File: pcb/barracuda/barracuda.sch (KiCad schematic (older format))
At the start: 79 parts, among them SW1 SW_PUSH, SW10 SW_PUSH, SW11 SW_PUSH, SW12 SW_PUSH, SW13 SW_PUSH, SW14 SW_PUSH, SW15 SW_PUSH, SW16 SW_PUSH, SW17 SW_PUSH, SW18 SW_PUSH, SW19 SW_PUSH, SW2 SW_PUSH, SW20 SW_PUSH, SW21 SW_PUSH, SW22 SW_PUSH, SW23 SW_PUSH, SW24 SW_PUSH, SW25 SW_PUSH, SW26 SW_PUSH, SW27 SW_PUSH, SW28 SW_PUSH, SW29 SW_PUSH, SW3 SW_PUSH, SW30 SW_PUSH, SW31 SW_PUSH, SW32 SW_PUSH, SW33 SW_PUSH, SW34 SW_PUSH, SW35 SW_PUSH, SW36 SW_PUSH, SW37 SW_PUSH, SW38 SW_PUSH, SW4 SW_PUSH, SW5 SW_PUSH, SW6 SW_PUSH, SW7 SW_PUSH, SW8 SW_PUSH, SW9 SW_PUSH, U1 ProMicro

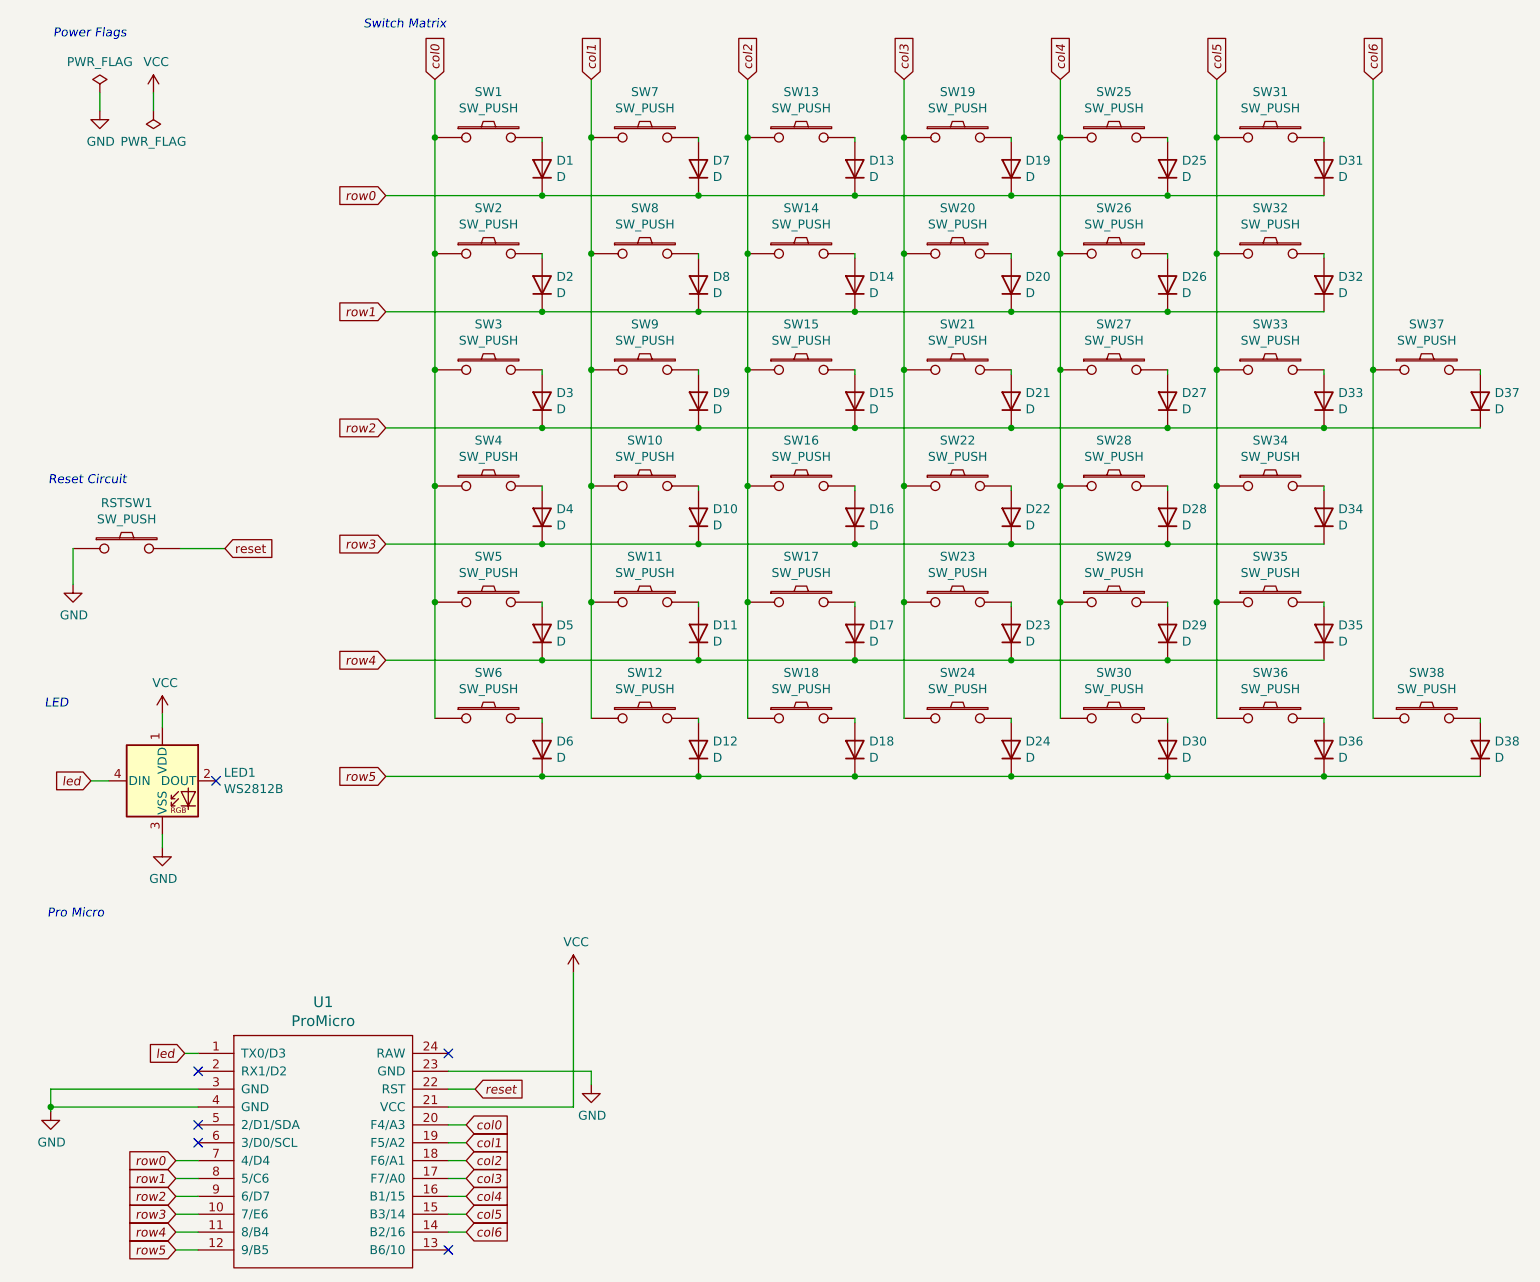
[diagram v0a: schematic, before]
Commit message: Reduced to 33 keys
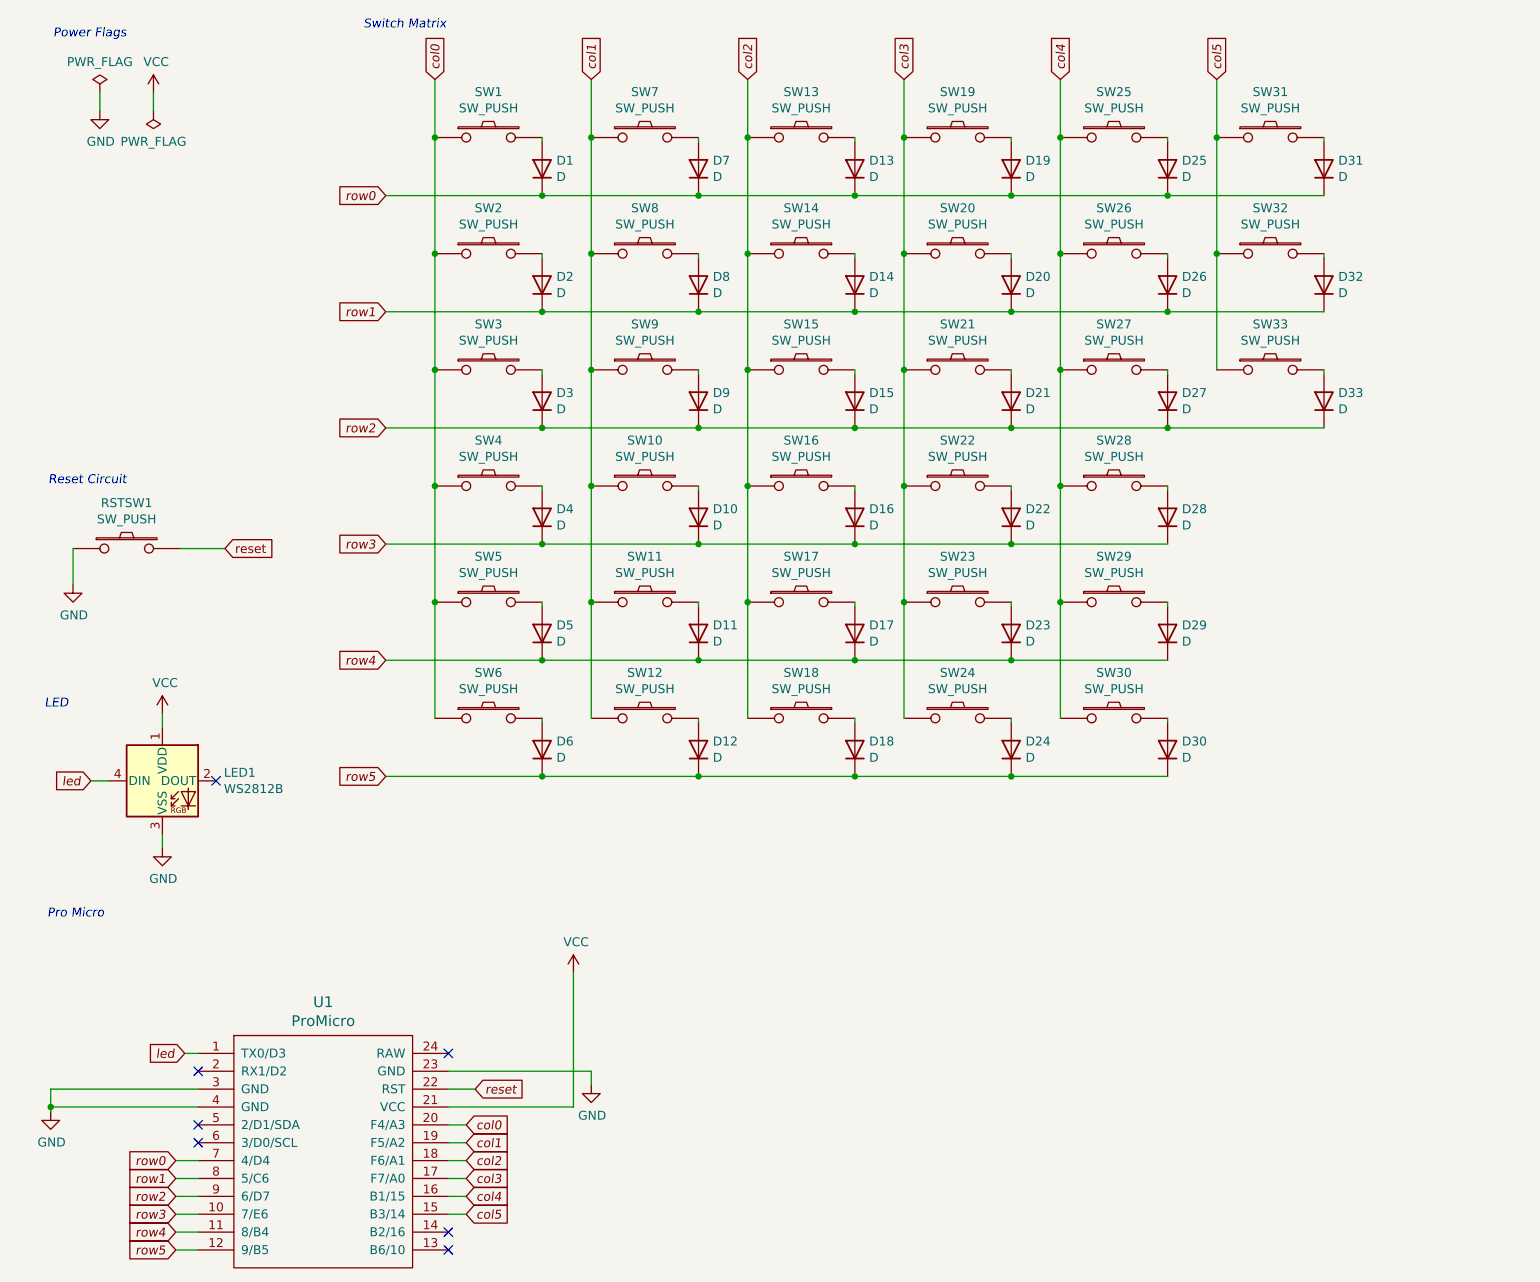
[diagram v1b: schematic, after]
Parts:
- removed D34, D35, D36, D37, D38: D, symbol Device:D
- removed SW34, SW35, SW36, SW37, SW38: SW_PUSH, symbol kbd:SW_PUSH
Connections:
- net col6: no longer names the net of U1.14 (B2/16)
- no-connect marks 6 -> 7
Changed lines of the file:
@@
 	7125 1900 7125 2550
 Connection ~ 7125 1900
-$Comp
-L kbd:SW_PUSH SW34
-U 1 1 5FB778EA
-P 7425 3200
-F 0 "SW34" H 7425 3455 50  0000 C CNN
-F 1 "SW_PUSH" H 7425 3364 50  0000 C CNN
-F 2 "" H 7425 3200 50  0000 C CNN
-F 3 "" H 7425 3200 50  0000 C CNN
-	1    7425 3200
-	1    0    0    -1
-$EndComp
-$Comp
-L Device:D D34
-U 1 1 5FB778F0
-P 7725 3375
-F 0 "D34" V 7771 3295 50  0000 R CNN
-F 1 "D" V 7680 3295 50  0000 R CNN
-F 2 "" H 7725 3375 50  0001 C CNN
-F 3 "~" H 7725 3375 50  0001 C CNN
-	1    7725 3375
-	0    -1   -1   0
-$EndComp
-Wire Wire Line
-	7725 3200 7725 3225
-$Comp
-L kbd:SW_PUSH SW35
-U 1 1 5FB778F7
-P 7425 3850
-F 0 "SW35" H 7425 4105 50  0000 C CNN
-F 1 "SW_PUSH" H 7425 4014 50  0000 C CNN
-F 2 "" H 7425 3850 50  0000 C CNN
-F 3 "" H 7425 3850 50  0000 C CNN
-	1    7425 3850
-	1    0    0    -1
-$EndComp
-$Comp
-L Device:D D35
-U 1 1 5FB778FD
-P 7725 4025
-F 0 "D35" V 7771 3945 50  0000 R CNN
-F 1 "D" V 7680 3945 50  0000 R CNN
-F 2 "" H 7725 4025 50  0001 C CNN
-F 3 "~" H 7725 4025 50  0001 C CNN
-	1    7725 4025
-	0    -1   -1   0
-$EndComp
-Wire Wire Line
-	7725 3850 7725 3875
-$Comp
-L kbd:SW_PUSH SW36
-U 1 1 5FB77904
-P 7425 4500
-F 0 "SW36" H 7425 4755 50  0000 C CNN
-F 1 "SW_PUSH" H 7425 4664 50  0000 C CNN
-F 2 "" H 7425 4500 50  0000 C CNN
-F 3 "" H 7425 4500 50  0000 C CNN
-	1    7425 4500
-	1    0    0    -1
-$EndComp
-$Comp
-L Device:D D36
-U 1 1 5FB7790A
-P 7725 4675
-F 0 "D36" V 7771 4595 50  0000 R CNN
-F 1 "D" V 7680 4595 50  0000 R CNN
-F 2 "" H 7725 4675 50  0001 C CNN
-F 3 "~" H 7725 4675 50  0001 C CNN
-	1    7725 4675
-	0    -1   -1   0
-$EndComp
-Wire Wire Line
-	7725 4500 7725 4525
-Wire Wire Line
-	7125 3200 7125 3850
-Wire Wire Line
-	7125 3850 7125 4500
-Connection ~ 7125 3850
 Text GLabel 7125 925  1    50   Input Italic 0
 col5
@@
 Wire Wire Line
 	7125 925  7125 1250
-Wire Wire Line
-	7125 2550 7125 3200
-Connection ~ 7125 2550
-Connection ~ 7125 3200
 Wire Wire Line
 	3350 1575 4225 1575
@@
 Connection ~ 5975 3525
 Wire Wire Line
-	6850 3525 7725 3525
-Connection ~ 6850 3525
-Wire Wire Line
-	7725 4175 6850 4175
-Wire Wire Line
 	6850 4175 5975 4175
-Connection ~ 6850 4175
 Wire Wire Line
 	5975 4175 5100 4175
@@
 	5975 4825 6850 4825
 Connection ~ 5975 4825
-Wire Wire Line
-	6850 4825 7725 4825
-Connection ~ 6850 4825
-$Comp
-L kbd:SW_PUSH SW37
-U 1 1 5FBED5C6
-P 8300 2550
-F 0 "SW37" H 8300 2805 50  0000 C CNN
-F 1 "SW_PUSH" H 8300 2714 50  0000 C CNN
-F 2 "" H 8300 2550 50  0000 C CNN
-F 3 "" H 8300 2550 50  0000 C CNN
-	1    8300 2550
-	1    0    0    -1
-$EndComp
-$Comp
-L Device:D D37
-U 1 1 5FBED5CC
-P 8600 2725
-F 0 "D37" V 8646 2645 50  0000 R CNN
-F 1 "D" V 8555 2645 50  0000 R CNN
-F 2 "" H 8600 2725 50  0001 C CNN
-F 3 "~" H 8600 2725 50  0001 C CNN
-	1    8600 2725
-	0    -1   -1   0
-$EndComp
-Wire Wire Line
-	8600 2550 8600 2575
-$Comp
-L kbd:SW_PUSH SW38
-U 1 1 5FBED5F0
-P 8300 4500
-F 0 "SW38" H 8300 4755 50  0000 C CNN
-F 1 "SW_PUSH" H 8300 4664 50  0000 C CNN
-F 2 "" H 8300 4500 50  0000 C CNN
-F 3 "" H 8300 4500 50  0000 C CNN
-	1    8300 4500
-	1    0    0    -1
-$EndComp
-$Comp
-L Device:D D38
-U 1 1 5FBED5F6
-P 8600 4675
-F 0 "D38" V 8646 4595 50  0000 R CNN
-F 1 "D" V 8555 4595 50  0000 R CNN
-F 2 "" H 8600 4675 50  0001 C CNN
-F 3 "~" H 8600 4675 50  0001 C CNN
-	1    8600 4675
-	0    -1   -1   0
-$EndComp
-Wire Wire Line
-	8600 4500 8600 4525
-Text GLabel 8000 925  1    50   Input Italic 0
-col6
-Connection ~ 8000 2550
-Wire Wire Line
-	8000 925  8000 2550
-Wire Wire Line
-	8000 2550 8000 4500
-Wire Wire Line
-	7725 2875 8600 2875
-Connection ~ 7725 2875
-Wire Wire Line
-	7725 4825 8600 4825
-Connection ~ 7725 4825
 Text GLabel 1300 6975 0    50   Input Italic 0
 row0
@@
 Text GLabel 2925 7275 2    50   Input Italic 0
 col5
-Text GLabel 2925 7375 2    50   Input Italic 0
-col6
 Wire Wire Line
 	2825 6775 2925 6775
@@
 Wire Wire Line
 	2825 7275 2925 7275
-Wire Wire Line
-	2825 7375 2925 7375
 Wire Wire Line
 	1300 6975 1425 6975
@@
 NoConn ~ 1425 6775
 NoConn ~ 1425 6475
+NoConn ~ 2825 7375
 $EndSCHEMATC

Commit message: Assigned footprint to each components
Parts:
- D1, D10, D11, D12, D13, D14, D15, D16, D17, D18, D19, D2, D20, D21, D22, D23, D24, D25, D26, D27, D28, D29, D3, D30, D31, D32, D33, D4, D5, D6, D7, D8, D9: footprint (none) -> kbd:D3_SMD
- RSTSW1: footprint (none) -> TVAF06-A020B-R:TVAF06-A020B-R
- SW1, SW10, SW11, SW12, SW13, SW14, SW15, SW16, SW17, SW18, SW19, SW2, SW20, SW21, SW22, SW23, SW24, SW25, SW26, SW27, SW28, SW29, SW3, SW30, SW31, SW32, SW33, SW4, SW5, SW6, SW7, SW8, SW9: footprint (none) -> kbd:CherryMX_Choc_Hotswap
- U1: footprint (none) -> Keebio-Parts:ArduinoProMicro
